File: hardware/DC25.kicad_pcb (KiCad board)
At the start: 2 copper layers, 18 parts, among them P2 CONN_01X04, SW1 SW_DPDT_x2, U1 ATMEGA328P-AU, Y1 16MHz

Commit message: Some progress
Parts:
- added G***: LOGO, images:p_logo_5_copper, F.Cu at (26.3, 64.6)
- added G***: LOGO, images:p_logo_5_mask, F.Cu at (26.3, 64.6)
- added G***: LOGO, footprints:bazooka_text, F.Cu at (41.4, 62.5)
- added G***: LOGO, footprints:bazooka, F.Cu at (56.3, 65.7)
- moved LED4 112.8 mm to (64.4, 18.9)
- moved U1 105.9 mm to (54.2, 41.8), turned to 225 degrees
- moved LED3 97.0 mm to (110.1, 18.9), turned to 135 degrees
- moved ISP1 93.1 mm to (68.2, 51.1)
- moved LED5 88.1 mm to (18.7, 18.9), turned to 225 degrees
- moved SW1 86.4 mm to (77.3, 29.8)
- moved LED2 84.8 mm to (110.1, 41.8)
- moved BT1 82.3 mm to (46.6, 54.5)
- moved P2 80.6 mm to (39.0, 51.9)
- moved DIS1 79.8 mm to (64.4, 41.8)
- moved LED6 76.3 mm to (18.7, 41.8)
- moved LED1 72.3 mm to (110.1, 64.6), turned to 45 degrees
- moved LED7 65.3 mm to (18.7, 64.6), turned to 315 degrees
- moved LED8 64.8 mm to (64.4, 64.6)
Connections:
- DIS1 pad 1: (no net) -> GND
- DIS1 pad 10: (no net) -> /DB3
- DIS1 pad 11: (no net) -> /DB4
- DIS1 pad 12: (no net) -> /DB5
- DIS1 pad 13: (no net) -> /DB6
- DIS1 pad 14: (no net) -> /DB7
- DIS1 pad 2: (no net) -> +5V
- DIS1 pad 3: (no net) -> Net-(DIS1-Pad3)
- DIS1 pad 4: (no net) -> /RS
- DIS1 pad 5: (no net) -> /RW
- DIS1 pad 6: (no net) -> /E
- DIS1 pad 7: (no net) -> /DB0
- DIS1 pad 8: (no net) -> /DB1
- DIS1 pad 9: (no net) -> /DB2
- U1 pad 1: /DB0 -> /DB7
- U1 pad 10: /DB3 -> /DB4
- U1 pad 11: /DB4 -> /DB3
- U1 pad 12: /DB5 -> /DB2
- U1 pad 13: /DB6 -> /DB1
- U1 pad 14: /DB7 -> /DB0
- U1 pad 2: /DB1 -> /DB6
- U1 pad 23: /RGB1 -> /E
- U1 pad 24: Net-(U1-Pad24) -> /RW
- U1 pad 25: Net-(U1-Pad25) -> /RS
- U1 pad 30: /RS -> /RGB1
- U1 pad 31: /RW -> Net-(U1-Pad31)
- U1 pad 32: /E -> Net-(U1-Pad32)
- U1 pad 9: /DB2 -> /DB5
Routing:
- net Net-(BT1-Pad2): track 0.00 -> 43.6 mm
- net GNDA: track 0.00 -> 43.0 mm
- net /RS: track 0.00 -> 34.9 mm
- net /RW: track 0.00 -> 29.2 mm
- net /E: track 0.00 -> 27.1 mm
- net /DB7: track 0.00 -> 18.2 mm
- net /DB6: track 0.00 -> 16.8 mm
- net /DB0: track 0.00 -> 15.7 mm
- net /DB5: track 0.00 -> 15.3 mm
- net /DB4: track 0.00 -> 15.0 mm
- net /DB3: track 0.00 -> 14.8 mm
- net /DB2: track 0.00 -> 14.5 mm
- net /DB1: track 0.00 -> 14.3 mm
- net +BATT: track 0.00 -> 2.54 mm
- net Net-(SW1-Pad3): track 0.00 -> 2.50 mm
- added copper zone on F.Cu, net +5V
- added copper zone on B.Cu, net GND
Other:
- board outline added: 101.6 x 55.9 mm
- board text added: "GrnzOnmbbxn"

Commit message: Some branding improvements
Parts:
- added G***: LOGO, footprints:bazooka_copper, F.Cu at (98.6, 64.5)
- added G***: LOGO, footprints:bazooka_text_copper, F.Cu at (79.7, 64.5)
- moved G*** 42.4 mm to (98.6, 64.5)
- moved G*** 38.4 mm to (79.7, 64.5)

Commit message: More branding and RGB signal, gnd lines.
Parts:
- added G***: LOGO, footprints:INV, F.Cu at (33.4, 64.6)
- added G***: LOGO, footprints:INV_copper, F.Cu at (33.4, 64.6)
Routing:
- net /RGB1: track 0.00 -> 69.1 mm, vias 0 -> 2
- net Net-(LED7-Pad2): track 0.00 -> 55.6 mm
- net Net-(LED4-Pad2): track 0.00 -> 47.7 mm
- net Net-(LED3-Pad2): track 0.00 -> 43.7 mm
- net Net-(LED6-Pad2): track 0.00 -> 29.7 mm
- net Net-(LED5-Pad2): track 0.00 -> 26.3 mm
- net Net-(LED2-Pad2): track 0.00 -> 24.9 mm
- net Net-(LED1-Pad2): track 0.00 -> 23.8 mm
- net +5V: track 0.00 -> 3.72 mm, vias 0 -> 2
- net GND: track 0.00 -> 0.42 mm, vias 0 -> 7
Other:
- board text added: "V gubhtug jung V'q qb jnf V'q cergraq V jnf bar bs"
- board text added: "Ynhtuvat Zna"
- board text added: "gubfr qrns-zhgrf"

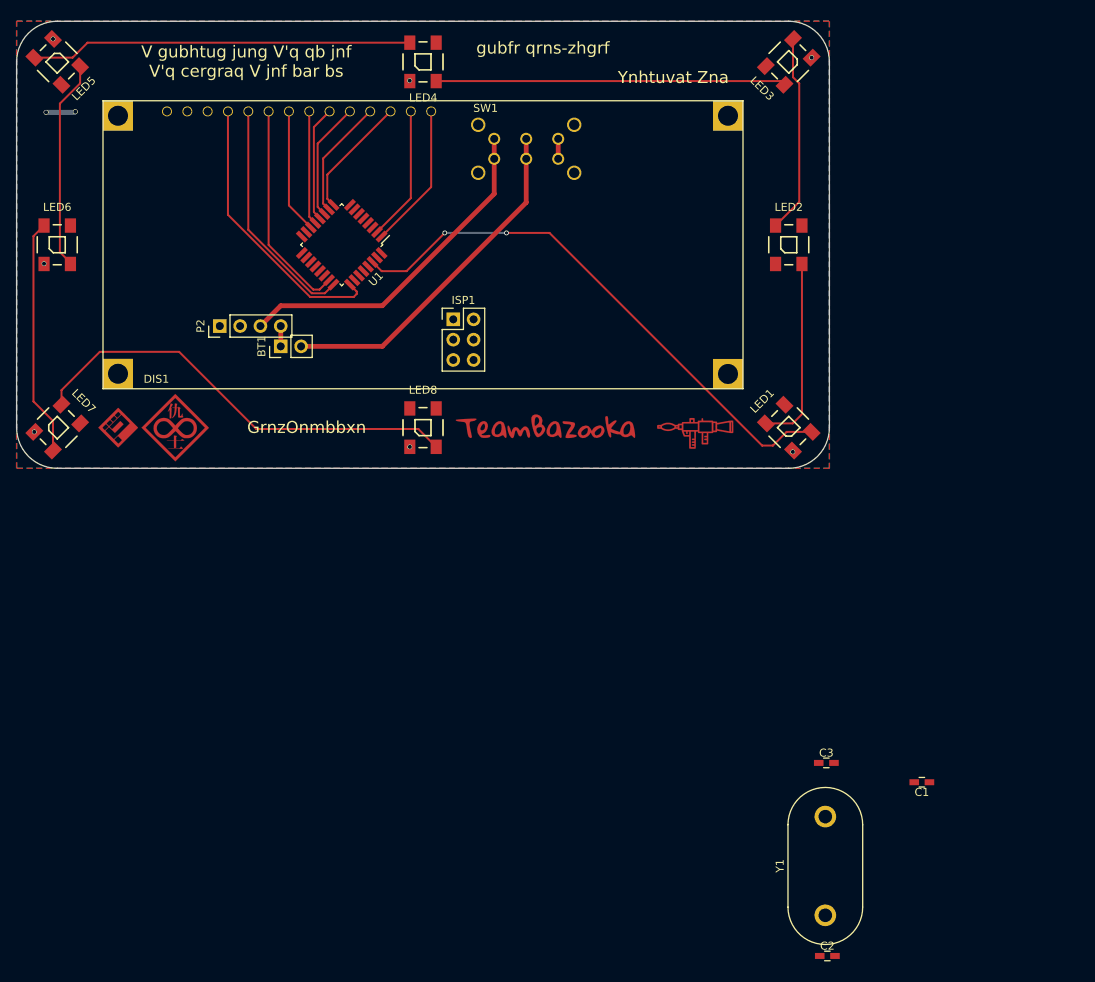
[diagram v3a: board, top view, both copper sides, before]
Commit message: Finish board layout.
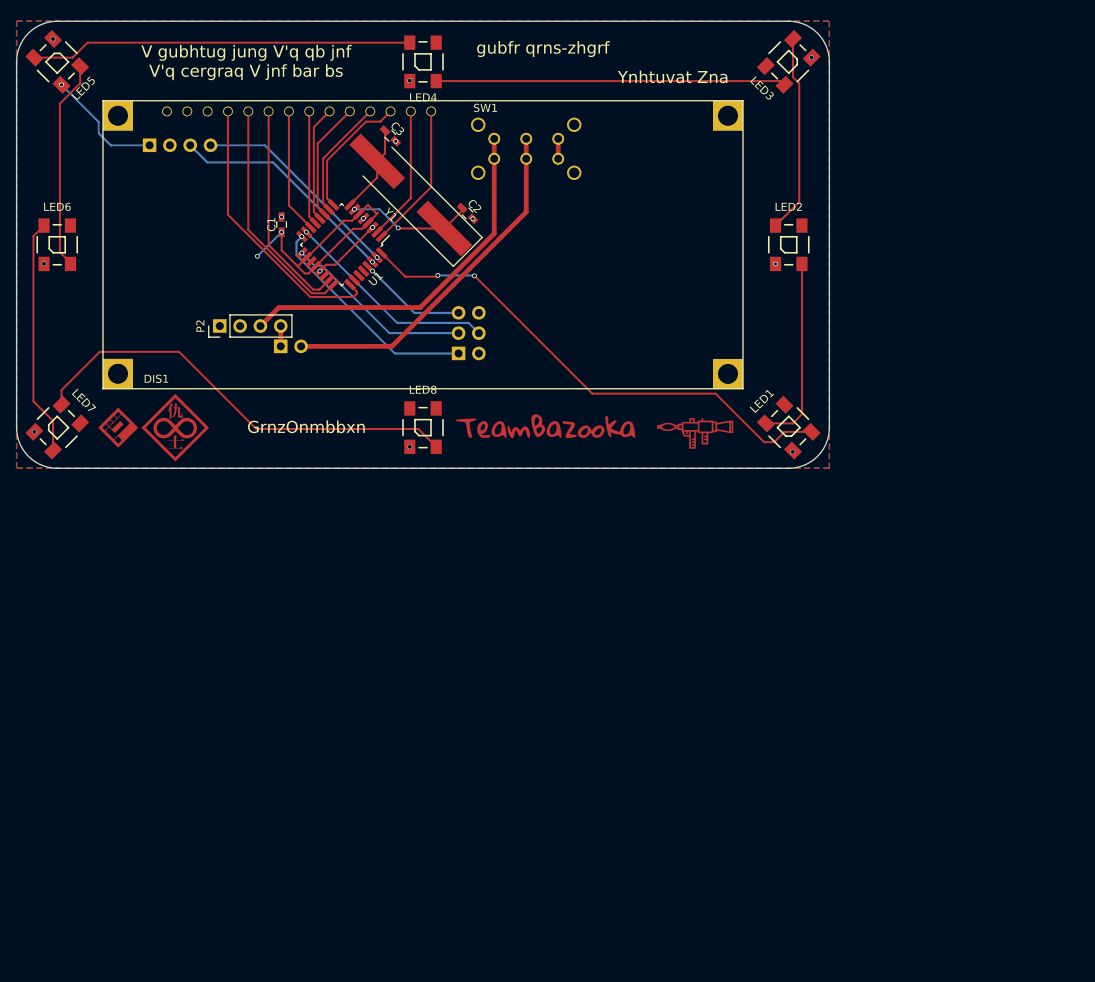
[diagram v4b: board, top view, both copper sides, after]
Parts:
- added P1: CONN_01X04, Pin_Headers:Pin_Header_Straight_1x04_Pitch2.54mm, B.Cu at (30.2, 29.3)
- BT1, ISP1: moved to B.Cu
- Y1: footprint Crystals:Crystal_HC33-U_Vertical -> Crystals:Crystal_SMD_HC49-SD_HandSoldering
- moved C1 106.1 mm to (46.7, 39.2), turned to 90 degrees
- moved Y1 103.9 mm to (62.9, 35.5), turned to 135 degrees
- moved C2 103.1 mm to (70.0, 37.9), turned to 315 degrees
- moved C3 95.5 mm to (60.3, 28.2), turned to 315 degrees
- moved ISP1 4.32 mm to (68.8, 55.4)
- turned BT1 to 270 degrees
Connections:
- U1 pad 30: /RGB1 -> /RX
- U1 pad 31: Net-(U1-Pad31) -> /TX
- U1 pad 32: Net-(U1-Pad32) -> /RGB1
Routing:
- net +5V: track 3.72 -> 51.7 mm, vias 2 -> 3
- net /RX: track 0.00 -> 28.8 mm, vias 0 -> 1
- net /ISP1: track 0.00 -> 27.9 mm, vias 0 -> 1
- net /ISP4: track 0.00 -> 26.8 mm, vias 0 -> 1
- net /TX: track 0.00 -> 26.6 mm, vias 0 -> 1
- net /ISP3: track 0.00 -> 23.7 mm, vias 0 -> 1
- net /CLK1: track 0.00 -> 15.7 mm, vias 0 -> 2
- net /ISP5: track 0.00 -> 13.7 mm, vias 0 -> 1
- net /CLK2: track 0.00 -> 11.1 mm
- net GND: track 0.42 -> 9.28 mm, vias 7 -> 14
- net /RGB1: track 69.1 -> 64.2 mm
- net GNDA: track 43.0 -> 45.9 mm
- net /DB5: track 15.3 -> 16.4 mm
- net Net-(BT1-Pad2): track 43.6 -> 44.3 mm

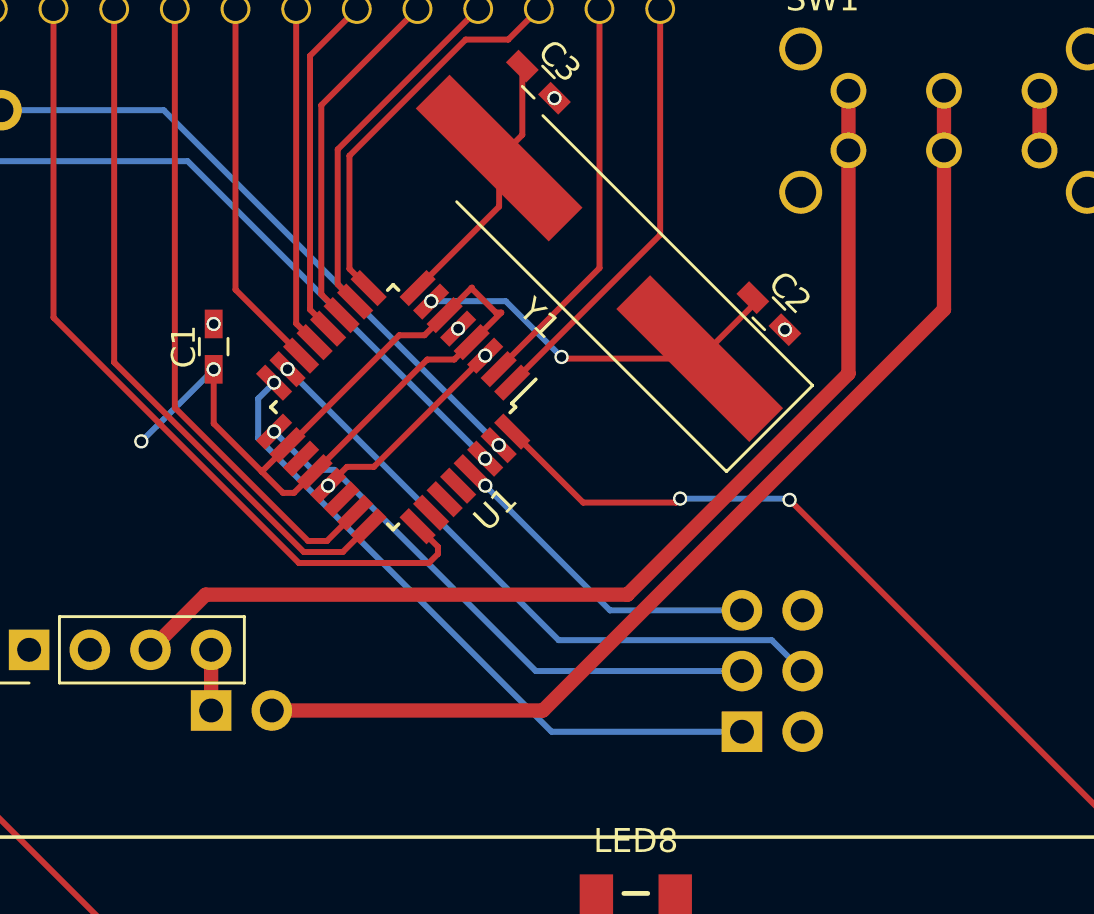
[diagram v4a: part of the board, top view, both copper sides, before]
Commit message: remove ground via, put swith on battery positive sideq
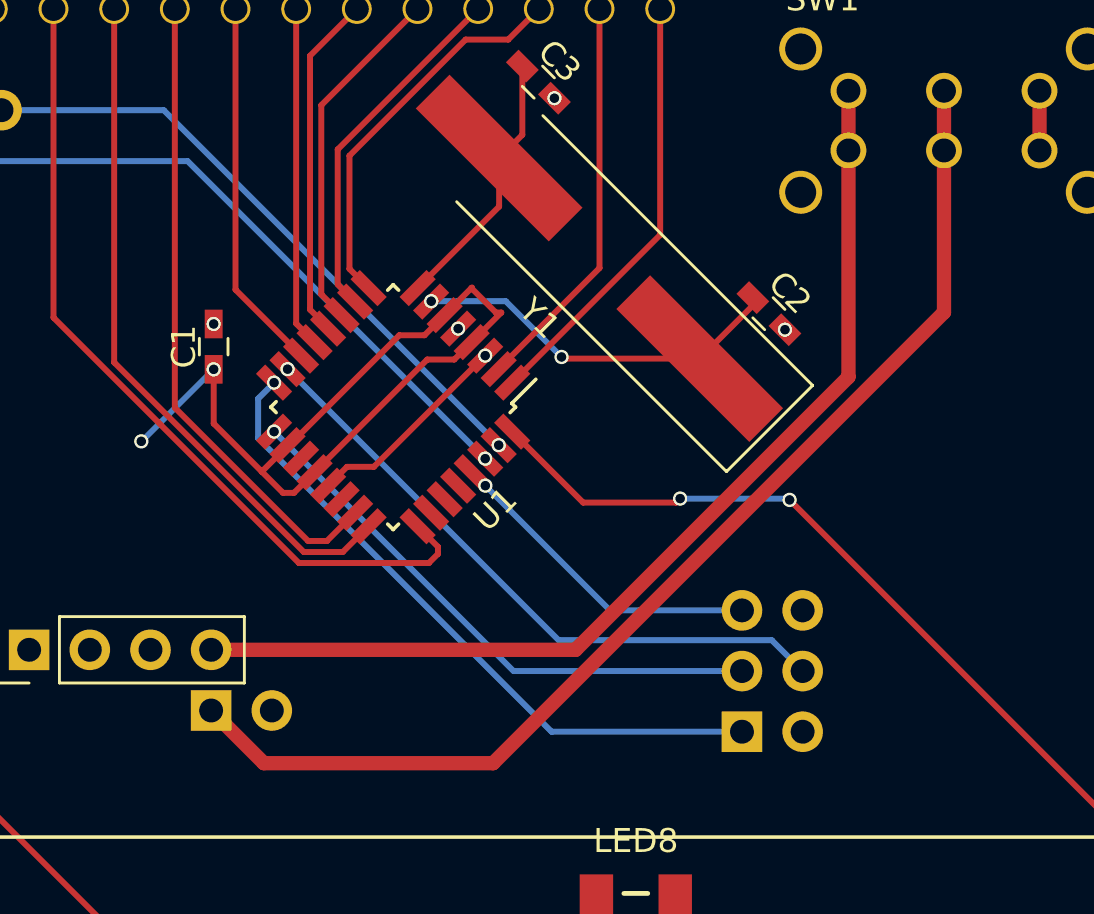
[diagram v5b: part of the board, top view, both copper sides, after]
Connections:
- BT1 pad 1: +BATT -> Net-(BT1-Pad1)
- BT1 pad 2: Net-(BT1-Pad2) -> GND
- P2 pad 3: GNDA -> GND
- SW1 pad 1: GNDA -> +BATT
- SW1 pad 2: Net-(BT1-Pad2) -> Net-(BT1-Pad1)
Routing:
- net Net-(BT1-Pad1): track 0.00 -> 48.7 mm
- net GNDA: track 45.9 -> 0.00 mm
- net Net-(BT1-Pad2): track 44.3 -> 0.00 mm
- net +BATT: track 2.54 -> 43.4 mm
- net GND: track 9.28 -> 9.27 mm, vias 14 -> 13

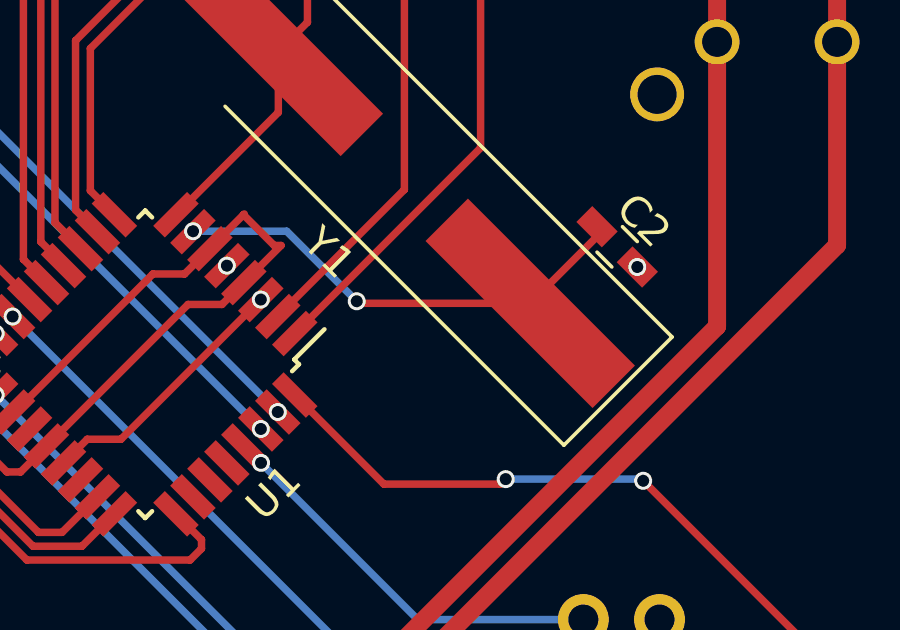
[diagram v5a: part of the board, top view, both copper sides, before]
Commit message: add battery holder mounting hole
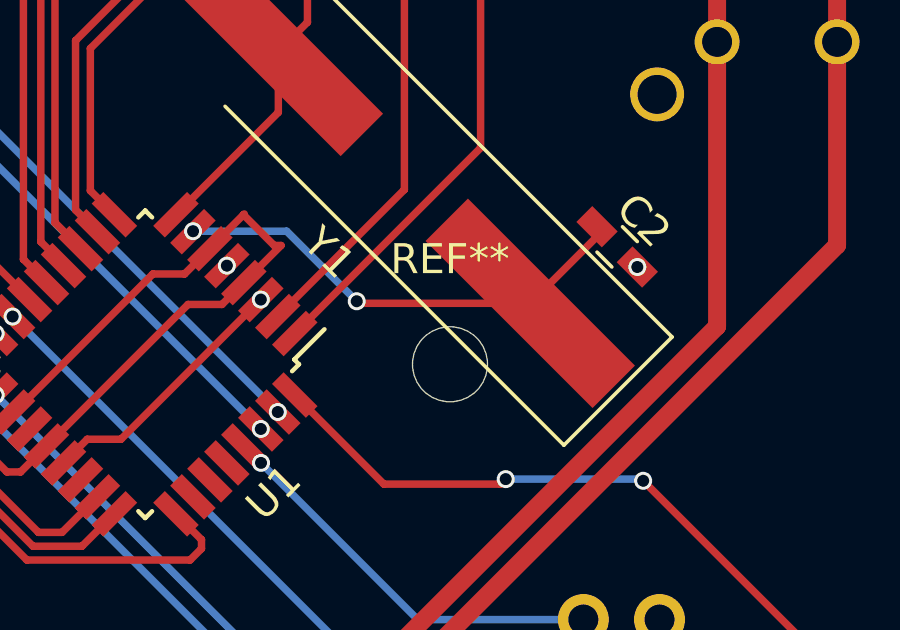
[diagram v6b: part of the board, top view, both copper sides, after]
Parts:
- added REF**: MountingHole_2.5mm, Mounting_Holes:MountingHole_2.5mm, F.Cu at (64.4, 41.8)
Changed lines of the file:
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@@
     (tracks 215)
     (zones 0)
-    (modules 27)
+    (modules 28)
     (nets 40)
   )
@@
     )
   )
+  (module Mounting_Holes:MountingHole_2.5mm (layer F.Cu)
+    (at 64.39 41.77)
+    (descr "Mounting Hole 2.5mm, no annular")
+    (tags "mounting hole 2.5mm no annular")
+    (fp_text reference REF** (at 0 -3.5) (layer F.SilkS)
+      (effects (font (size 1 1) (thickness 0.15)))
+    )
+    (fp_text value MountingHole_2.5mm (at 0 3.5) (layer F.Fab)
+      (effects (font (size 1 1) (thickness 0.15)))
+    )
+    (fp_circle (center 0 0) (end 2.5 0) (layer Cmts.User) (width 0.15))
+    (fp_circle (center 0 0) (end 2.75 0) (layer F.CrtYd) (width 0.05))
+    (pad 1 np_thru_hole circle (at 0 0) (size 2.5 2.5) (drill 2.5) (layers *.Cu *.Mask))
+  )
   (gr_text "Ynhtuvat Zna" (at 95.6828 20.85564) (layer F.SilkS)
     (effects (font (size 1.5 1.5) (thickness 0.3)))
@@
   (gr_arc (start 110.11 18.91) (end 110.11 13.83) (angle 90) (layer Edge.Cuts) (width 0.15))
   (gr_arc (start 18.67 18.91) (end 13.59 18.91) (angle 90) (layer Edge.Cuts) (width 0.15))
-  (segment (start 73.2932 31.02358) (end 73.2932 40.50712) (width 0.6) (layer F.Cu) (net 1) (status 400000))
-  (segment (start 61.87032 51.93) (end 46.61 51.93) (width 0.6) (layer F.Cu) (net 1) (status 800000))
+  (segment (start 73.2932 31.02358) (end 73.2932 40.50712) (width 0.6) (layer F.Cu) (net 1))
+  (segment (start 61.87032 51.93) (end 46.61 51.93) (width 0.6) (layer F.Cu) (net 1))
   (segment (start 73.2932 40.50712) (end 61.87032 51.93) (width 0.6) (layer F.Cu) (net 1))
   (segment (start 73.2932 28.52358) (end 73.2932 31.02358) (width 0.6) (layer F.Cu) (net 1))
@@
   (segment (start 45.627356 31.4703) (end 37.4279 31.4703) (width 0.25) (layer B.Cu) (net 38))
   (segment (start 45.627356 31.4703) (end 58.083732 43.926676) (width 0.25) (layer B.Cu) (net 38))
-  (segment (start 77.2932 31.02358) (end 77.2932 37.79998) (width 0.6) (layer F.Cu) (net 39) (status 400000))
-  (segment (start 48.81726 56.67726) (end 46.61 54.47) (width 0.6) (layer F.Cu) (net 39) (status 800000))
+  (segment (start 77.2932 31.02358) (end 77.2932 37.79998) (width 0.6) (layer F.Cu) (net 39))
+  (segment (start 48.81726 56.67726) (end 46.61 54.47) (width 0.6) (layer F.Cu) (net 39))
   (segment (start 58.41592 56.67726) (end 48.81726 56.67726) (width 0.6) (layer F.Cu) (net 39))
   (segment (start 77.2932 37.79998) (end 58.41592 56.67726) (width 0.6) (layer F.Cu) (net 39))
